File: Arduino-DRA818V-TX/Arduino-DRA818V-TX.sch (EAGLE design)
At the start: 22 parts, among them M1 ARDUINO_R3_ICSP, X1 SMA, X2 SMA

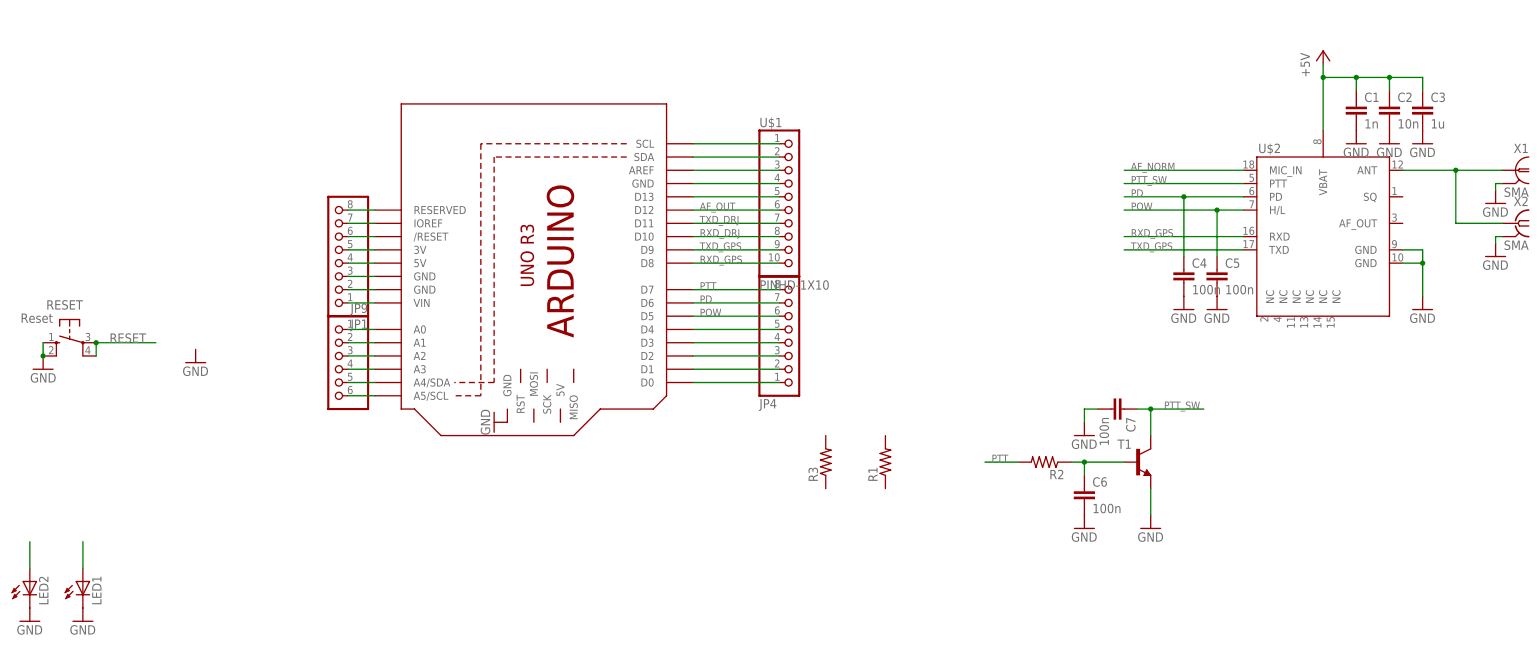
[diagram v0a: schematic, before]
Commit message: Adding Arduino-DRA818V-TX
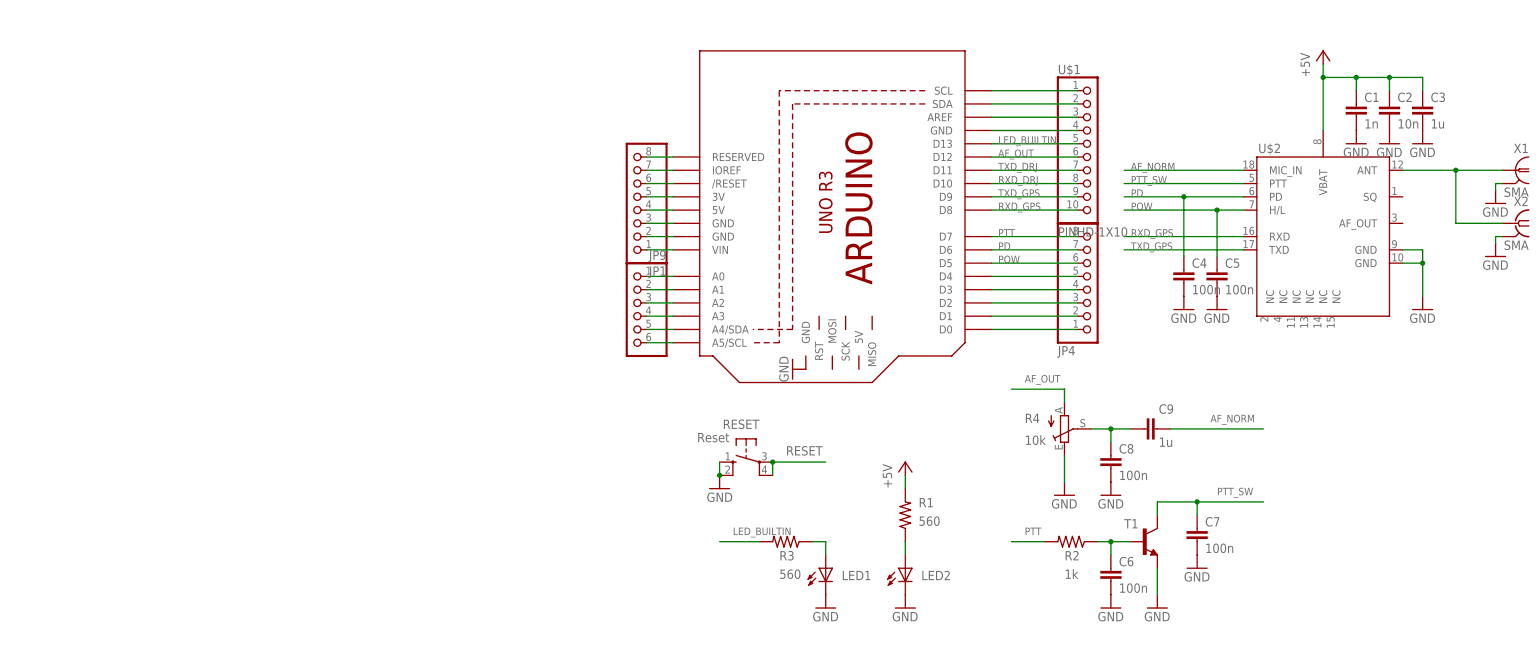
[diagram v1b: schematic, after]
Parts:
- added C8: 100n, resistor:C-EUC1206
- added C9: 1u, resistor:C-EUC1206
- added R4: 10k, pot:TRIM_EU-CA6V
- R1, R3: value (none) -> 560
- R2: value (none) -> 1k
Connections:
- removed net N$18: JP1.6, M1./RESET
- removed net N$6: M1.D13, U$1.5
- new net LED_BUILTIN: M1.D13, R3.2, U$1.5
- new net N$9: C8.1, C9.1, R4.S
- net +5V: now also R1.2
- net AF_NORM: now also C9.2
- net AF_OUT: now also R4.A
- net GND: now also C8.2, R4.E
- net N$41: now also R1.1
- net N$8: now also R3.1
- net RESET: now also JP1.6, M1./RESET
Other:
- moved on the sheet: C6, C7, JP1, JP4, JP9, LED1, LED2, R1, R2, R3, RESET, T1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

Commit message: Adding Arduino-DRA818V-TX
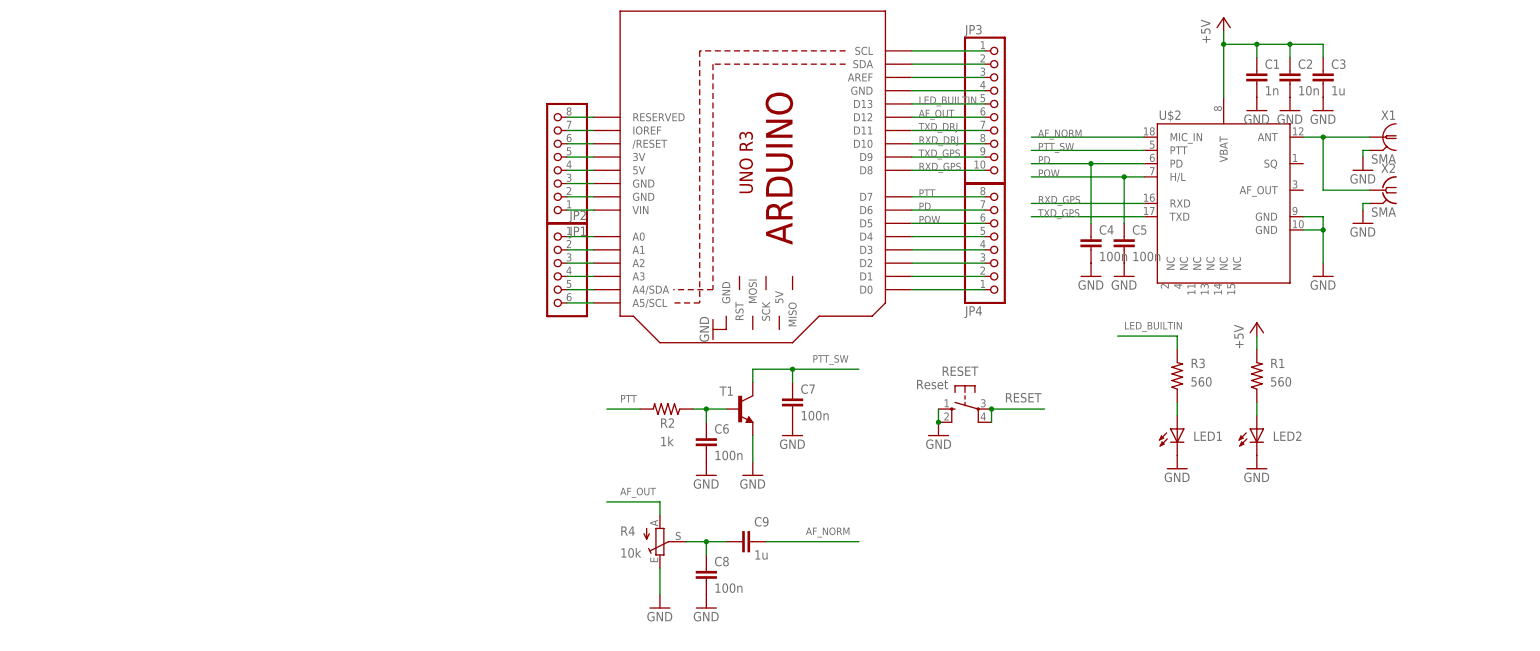
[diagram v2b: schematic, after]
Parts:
- removed JP9: (no value), carduino:PINHD-1X6B
- removed U$1: PINHD-1X10, adafruit:PINHD-1X10
- added JP2: (no value), carduino:PINHD-1X6B
- added JP3: PINHD-1X10, adafruit:PINHD-1X10
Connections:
- net AF_OUT: now also JP3.6; no longer U$1.6
- net GND: now also JP3.4; no longer U$1.4
- net LED_BUILTIN: now also JP3.5; no longer U$1.5
- net N$1: now also JP3.1; no longer U$1.1
- net N$2: now also JP3.2; no longer U$1.2
- net N$21: now also JP2.1; no longer JP9.1
- net N$22: now also JP2.2; no longer JP9.2
- net N$23: now also JP2.3; no longer JP9.3
- net N$24: now also JP2.4; no longer JP9.4
- net N$25: now also JP2.5; no longer JP9.5
- net N$26: now also JP2.6; no longer JP9.6
- net N$3: now also JP3.3; no longer U$1.3
- net RXD_DRJ: now also JP3.8; no longer U$1.8
- net RXD_GPS: now also JP3.10; no longer U$1.10
- net TXD_DRJ: now also JP3.7; no longer U$1.7
- net TXD_GPS: now also JP3.9; no longer U$1.9
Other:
- moved on the sheet: C1, C2, C3, C4, C5, C6, C7, C8, C9, JP1, JP4, LED1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

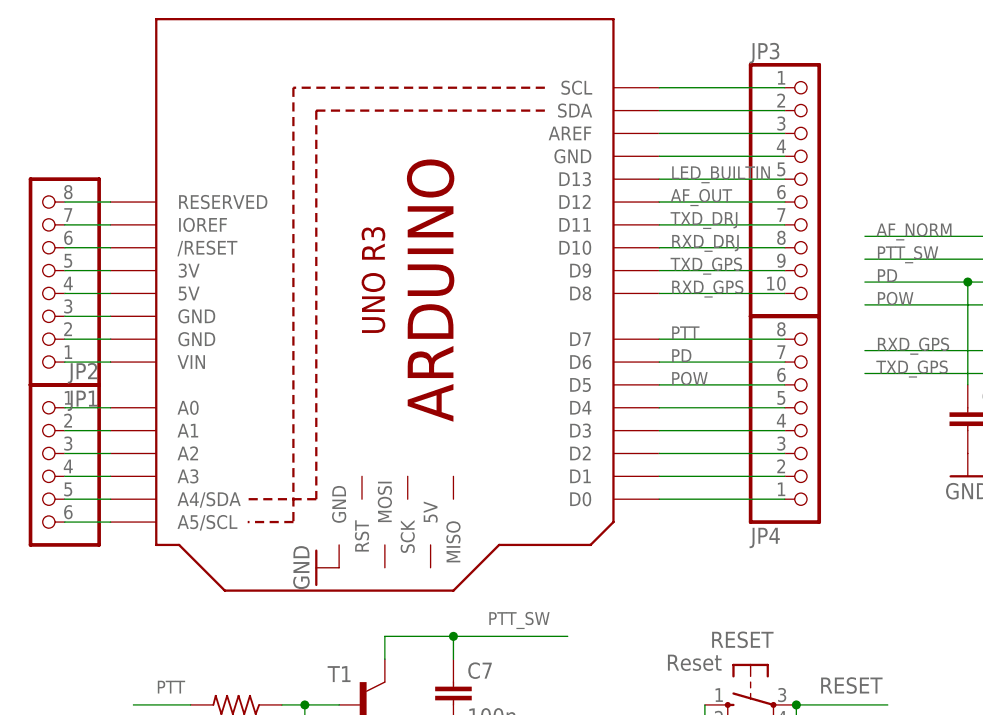
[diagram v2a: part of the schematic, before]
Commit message: Removing Female header
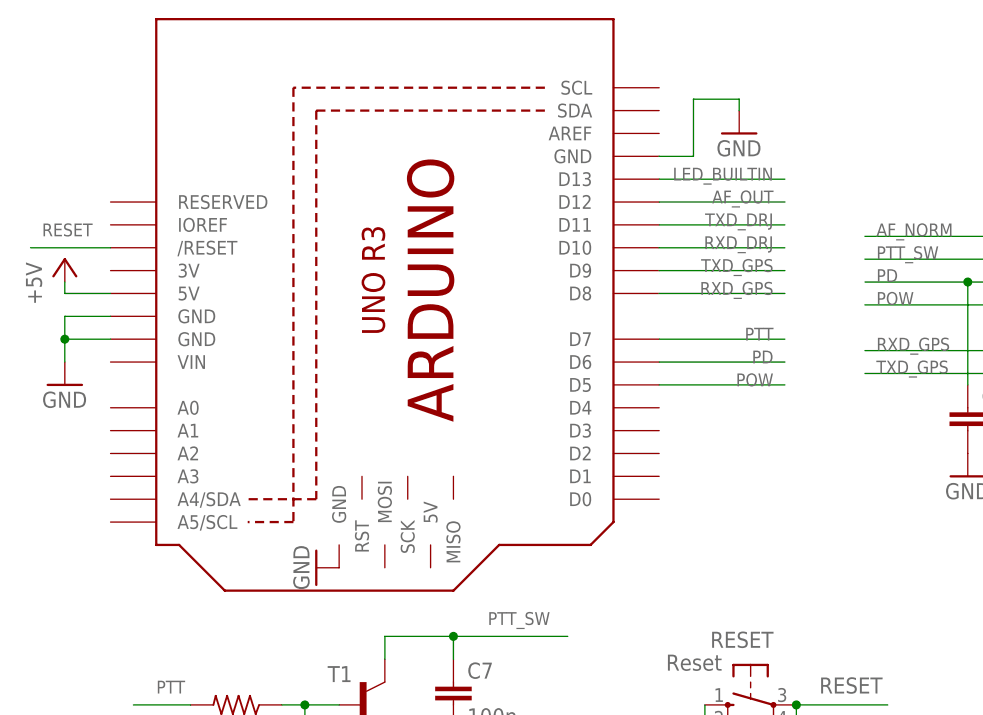
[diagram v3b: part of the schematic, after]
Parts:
- removed JP1, JP4: (no value), carduino:PINHD-1X8BIG
- removed JP2: (no value), carduino:PINHD-1X6B
- removed JP3: PINHD-1X10, adafruit:PINHD-1X10
- T1: device transistor:BC547A-NPN-TO92-CBE -> transistor:MMBT3904LT1-NPN-SOT23-BEC
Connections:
- removed net N$1: JP3.1, M1.SCL
- removed net N$17: JP1.5, M1.3V
- removed net N$19: JP1.7, M1.IOREF
- removed net N$2: JP3.2, M1.SDA
- removed net N$20: JP1.8, M1.RESERVED
- removed net N$21: JP2.1, M1.A0
- removed net N$22: JP2.2, M1.A1
- removed net N$23: JP2.3, M1.A2
- removed net N$24: JP2.4, M1.A3
- removed net N$25: JP2.5, M1.A4/SDA
- removed net N$26: JP2.6, M1.A5/SCL
- removed net N$27: JP4.1, M1.D0
- removed net N$28: JP4.2, M1.D1
- removed net N$29: JP4.3, M1.D2
- removed net N$3: JP3.3, M1.AREF
- removed net N$30: JP4.4, M1.D3
- removed net N$31: JP4.5, M1.D4
- removed net N$4: JP1.1, M1.VIN
- net +5V: no longer JP1.4
- net AF_OUT: no longer JP3.6
- net GND: no longer JP1.2, JP1.3, JP3.4
- net LED_BUILTIN: no longer JP3.5
- net PD: no longer JP4.7
- net POW: no longer JP4.6
- net PTT: no longer JP4.8
- net RESET: no longer JP1.6
- net RXD_DRJ: no longer JP3.8
- net RXD_GPS: no longer JP3.10
- net TXD_DRJ: no longer JP3.7
- net TXD_GPS: no longer JP3.9

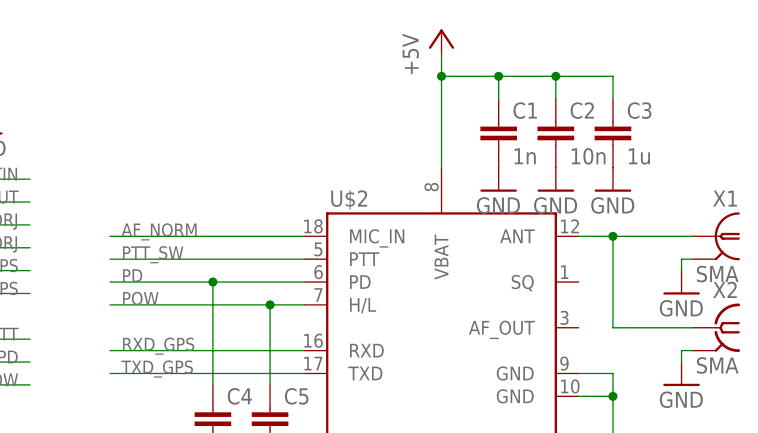
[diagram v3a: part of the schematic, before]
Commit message: Apply SparkFun DRU
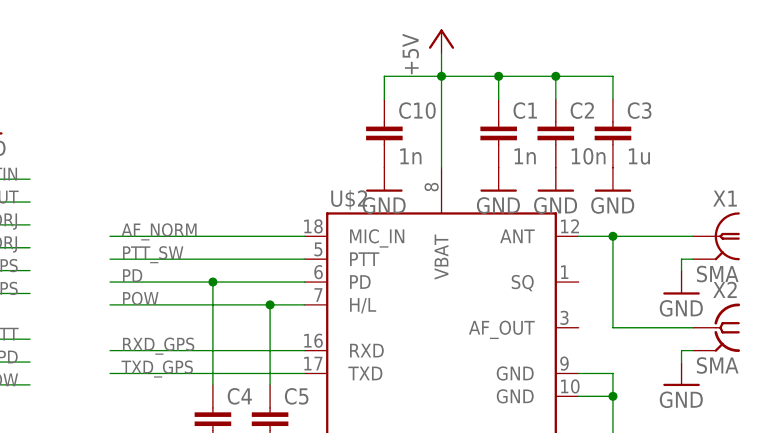
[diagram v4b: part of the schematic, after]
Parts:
- added C10: 1n, resistor:C-EUC1206
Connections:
- net +5V: now also C10.1
- net GND: now also C10.2
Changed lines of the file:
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@@
 <part name="GND19" library="supply1" deviceset="GND" device=""/>
 <part name="T1" library="transistor" deviceset="*-NPN-" device="SOT23-BEC" technology="MMBT3904LT1"/>
+<part name="C10" library="resistor" deviceset="C-EU" device="C1206" value="1n"/>
+<part name="GND20" library="supply1" deviceset="GND" device=""/>
 </parts>
 <sheets>
@@
 <attribute name="VALUE" x="38.1" y="54.61" size="1.778" layer="96"/>
 </instance>
+<instance part="C10" gate="G$1" x="134.62" y="114.3"/>
+<instance part="GND20" gate="1" x="134.62" y="106.68"/>
 </instances>
 <busses>
@@
 <wire x1="153.67" y1="116.84" x2="153.67" y2="119.38" width="0.1524" layer="91"/>
 <junction x="153.67" y="119.38"/>
+<pinref part="C10" gate="G$1" pin="1"/>
+<wire x1="140.97" y1="119.38" x2="134.62" y2="119.38" width="0.1524" layer="91"/>
+<wire x1="134.62" y1="119.38" x2="134.62" y2="116.84" width="0.1524" layer="91"/>
 </segment>
 <segment>
@@
 <wire x1="85.09" y1="116.84" x2="85.09" y2="110.49" width="0.1524" layer="91"/>
 <wire x1="85.09" y1="110.49" x2="81.28" y2="110.49" width="0.1524" layer="91"/>
+<pinref part="GND19" gate="1" pin="GND"/>
 </segment>
 <segment>
@@
 <wire x1="33.02" y1="13.97" x2="33.02" y2="19.05" width="0.1524" layer="91"/>
 </segment>
+<segment>
+<pinref part="C10" gate="G$1" pin="2"/>
+<pinref part="GND20" gate="1" pin="GND"/>
+</segment>
 </net>
 <net name="RESET" class="0">
@@
 </sheet>
 </sheets>
-<errors>
-</errors>
 </schematic>
 </drawing>

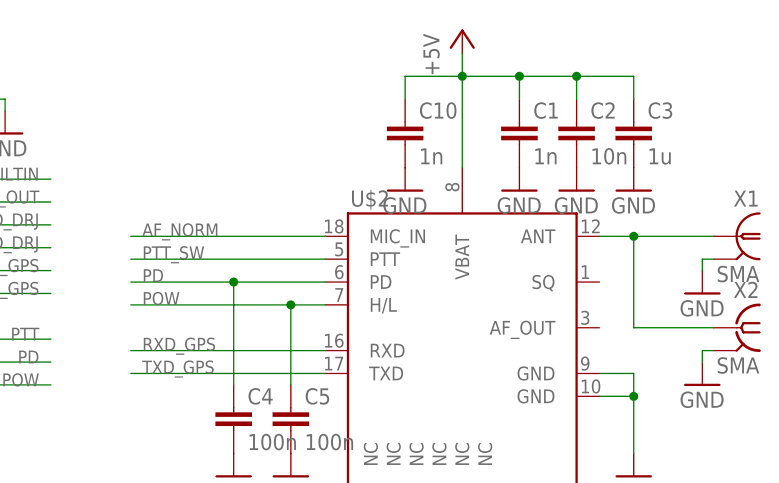
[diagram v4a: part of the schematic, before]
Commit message: Apply Polygon Pour
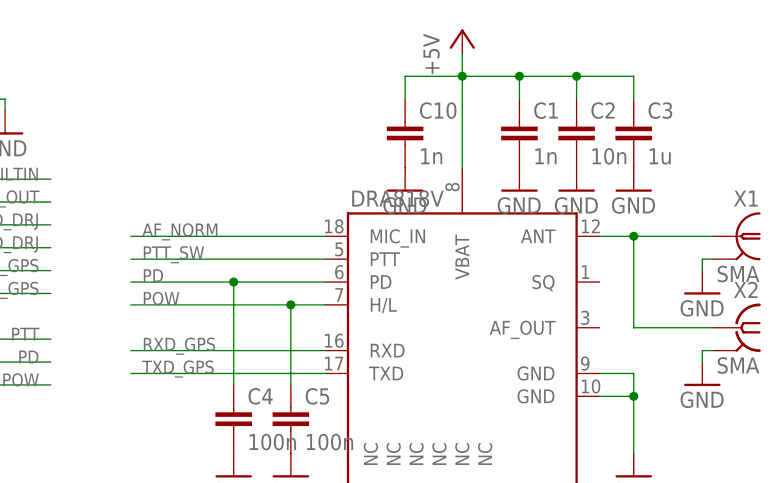
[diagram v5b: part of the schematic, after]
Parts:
- renumbered U$2 to DRA818V
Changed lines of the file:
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@@
 <part name="GND3" library="supply1" deviceset="GND" device=""/>
 <part name="GND10" library="supply1" deviceset="GND" device=""/>
-<part name="U$2" library="dorji" deviceset="DRA818A" device=""/>
+<part name="DRA818V" library="dorji" deviceset="DRA818A" device=""/>
 <part name="R1" library="resistor" deviceset="R-US_" device="R1206" value="560"/>
 <part name="R2" library="resistor" deviceset="R-US_" device="R1206" value="1k"/>
@@
 <instance part="GND3" gate="1" x="43.18" y="64.77" rot="R270"/>
 <instance part="GND10" gate="1" x="160.02" y="74.93"/>
-<instance part="U$2" gate="G$1" x="140.97" y="88.9"/>
+<instance part="DRA818V" gate="G$1" x="140.97" y="88.9"/>
 <instance part="R1" gate="G$1" x="147.32" y="55.88" smashed="yes" rot="R90">
 <attribute name="NAME" x="149.86" y="57.3786" size="1.778" layer="95"/>
@@
 </segment>
 <segment>
-<pinref part="U$2" gate="G$1" pin="VBAT"/>
+<pinref part="DRA818V" gate="G$1" pin="VBAT"/>
 <pinref part="P+1" gate="1" pin="+5V"/>
 <wire x1="140.97" y1="121.92" x2="140.97" y2="119.38" width="0.1524" layer="91"/>
@@
 </segment>
 <segment>
-<pinref part="U$2" gate="G$1" pin="GND@1"/>
+<pinref part="DRA818V" gate="G$1" pin="GND@1"/>
 <pinref part="GND10" gate="1" pin="GND"/>
 <wire x1="156.21" y1="86.36" x2="160.02" y2="86.36" width="0.1524" layer="91"/>
 <wire x1="160.02" y1="86.36" x2="160.02" y2="83.82" width="0.1524" layer="91"/>
-<pinref part="U$2" gate="G$1" pin="GND@2"/>
+<pinref part="DRA818V" gate="G$1" pin="GND@2"/>
 <wire x1="160.02" y1="83.82" x2="160.02" y2="77.47" width="0.1524" layer="91"/>
 <wire x1="156.21" y1="83.82" x2="160.02" y2="83.82" width="0.1524" layer="91"/>
@@
 </segment>
 <segment>
-<pinref part="U$2" gate="G$1" pin="TXD"/>
+<pinref part="DRA818V" gate="G$1" pin="TXD"/>
 <wire x1="125.73" y1="86.36" x2="104.14" y2="86.36" width="0.1524" layer="91"/>
 <label x="105.41" y="86.36" size="1.4224" layer="95"/>
@@
 </segment>
 <segment>
-<pinref part="U$2" gate="G$1" pin="RXD"/>
+<pinref part="DRA818V" gate="G$1" pin="RXD"/>
 <wire x1="125.73" y1="88.9" x2="104.14" y2="88.9" width="0.1524" layer="91"/>
 <label x="105.41" y="88.9" size="1.4224" layer="95"/>
@@
 </segment>
 <segment>
-<pinref part="U$2" gate="G$1" pin="H/L"/>
+<pinref part="DRA818V" gate="G$1" pin="H/L"/>
 <wire x1="125.73" y1="93.98" x2="121.92" y2="93.98" width="0.1524" layer="91"/>
 <pinref part="C5" gate="G$1" pin="1"/>
@@
 </segment>
 <segment>
-<pinref part="U$2" gate="G$1" pin="PD"/>
+<pinref part="DRA818V" gate="G$1" pin="PD"/>
 <wire x1="125.73" y1="96.52" x2="115.57" y2="96.52" width="0.1524" layer="91"/>
 <pinref part="C4" gate="G$1" pin="1"/>
@@
 <net name="PTT_SW" class="0">
 <segment>
-<pinref part="U$2" gate="G$1" pin="PTT"/>
+<pinref part="DRA818V" gate="G$1" pin="PTT"/>
 <wire x1="125.73" y1="99.06" x2="104.14" y2="99.06" width="0.1524" layer="91"/>
 <label x="105.41" y="99.06" size="1.4224" layer="95"/>
@@
 <net name="AF_NORM" class="0">
 <segment>
-<pinref part="U$2" gate="G$1" pin="MIC_IN"/>
+<pinref part="DRA818V" gate="G$1" pin="MIC_IN"/>
 <wire x1="125.73" y1="101.6" x2="104.14" y2="101.6" width="0.1524" layer="91"/>
 <label x="105.41" y="101.6" size="1.4224" layer="95"/>
@@
 <net name="N$5" class="0">
 <segment>
-<pinref part="U$2" gate="G$1" pin="ANT"/>
+<pinref part="DRA818V" gate="G$1" pin="ANT"/>
 <pinref part="X1" gate="G$1" pin="1"/>
 <wire x1="156.21" y1="101.6" x2="160.02" y2="101.6" width="0.1524" layer="91"/>
